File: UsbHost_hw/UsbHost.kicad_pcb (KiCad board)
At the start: 2 copper layers, 24 x 72 mm, 41 parts, among them Q1 LED_RGB, SW1 BUTTON

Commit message: + USBHost HW v3
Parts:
- removed C23: 1.8pF, Capacitors:CAP_0402
- removed R7: 51R, Resistors:RES_0603
- removed XL2: ST_SWD, Connectors:PLS-4
- added C11: 1u, Capacitors:CAP_0603, F.Cu at (169.8, 161.0)
- added C9: 18pF, Capacitors:CAP_0603, F.Cu at (188.3, 180.6)
- added DA2: MCP1700, SOT:SOT23-3, F.Cu at (169.4, 189.7)
- added Logo1: Logo, Pictures:Ostranna_16d9_13d5, F.Cu at (178.5, 135.8)
- added R4: 100R, Resistors:RES_0603, F.Cu at (173.0, 169.6)
- added XTAL1: 12MHz, Quartz:0503x4-4, F.Cu at (188.3, 176.4)
- C1: value 10n -> 18pF
- C12, C14: value 10pF -> 18pF
- C16, C21: value 220pF -> 0.1u
- C17, C19: value 10n -> 0.1u
- C18: value 3.3pF -> 0.1u
- C22: value 1.8pF -> 2.7pF
- C3: footprint Capacitors:CAP_0805 -> Capacitors:CAP_0603
- Q1: value LED_RGB -> LED_5050
- R1: value 1M -> 100R
- R3: value 51R -> 100R
- R6: value 51R -> 1k
- XL1: value CONN_3 -> CONN_6; footprint Connectors:PLS-3 -> Connectors:PLS-6
- moved C1 25.3 mm to (188.3, 172.3), turned to 0 degrees
- moved R1 25.0 mm to (173.0, 166.4)
- moved C13 23.3 mm to (169.3, 187.9)
- moved DA1 23.1 mm to (169.3, 189.9)
- moved C10 19.5 mm to (171.8, 189.7), turned to 90 degrees
- moved R6 15.1 mm to (184.8, 175.9)
- moved XL1 13.0 mm to (168.7, 184.2), turned to 90 degrees
- moved TP2 12.9 mm to (182.3, 171.7)
- moved C2 11.4 mm to (176.8, 182.6)
- moved C3 8.02 mm to (185.6, 179.8), turned to 270 degrees
- moved C8 1.68 mm to (184.0, 179.8), turned to 270 degrees
- moved C7 1.68 mm to (184.1, 173.6), turned to 90 degrees
- moved R2 0.91 mm to (188.1, 183.7)
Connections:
- C1 pad 1: /SHLD -> Net-(C1-Pad1)
- DD1 pad 10: (no net) -> Net-(DD1-Pad10)
- DD1 pad 11: (no net) -> Net-(DD1-Pad11)
- DD1 pad 2: (no net) -> Net-(DD1-Pad2)
- DD1 pad 20: (no net) -> Net-(DD1-Pad20)
- DD1 pad 21: (no net) -> Net-(DD1-Pad21)
- DD1 pad 22: (no net) -> Net-(DD1-Pad22)
- DD1 pad 25: (no net) -> Net-(DD1-Pad25)
- DD1 pad 26: (no net) -> Net-(DD1-Pad26)
- DD1 pad 27: (no net) -> Net-(DD1-Pad27)
- DD1 pad 28: (no net) -> Net-(DD1-Pad28)
- DD1 pad 29: (no net) -> Net-(DD1-Pad29)
- DD1 pad 3: (no net) -> Net-(DD1-Pad3)
- DD1 pad 38: (no net) -> Net-(DD1-Pad38)
- DD1 pad 39: (no net) -> Net-(DD1-Pad39)
- DD1 pad 4: (no net) -> Net-(DD1-Pad4)
- DD1 pad 41: (no net) -> Net-(DD1-Pad41)
- DD1 pad 42: (no net) -> Net-(DD1-Pad42)
- DD1 pad 43: (no net) -> Net-(DD1-Pad43)
- DD1 pad 45: (no net) -> Net-(DD1-Pad45)
- DD1 pad 46: (no net) -> Net-(DD1-Pad46)
- DD1 pad 5: (no net) -> Net-(C9-Pad1)
- DD1 pad 6: (no net) -> Net-(DD1-Pad6)
- DD1 pad 7: (no net) -> Net-(DD1-Pad7)
- R1 pad 1: /SHLD -> Net-(Q1-Pad1)
- R1 pad 2: GND -> /LED_G
- R3 pad 1: Net-(Q1-PadRA) -> Net-(Q1-Pad2)
- R6 pad 1: Net-(Q1-PadGA) -> Net-(C1-Pad1)
- R6 pad 2: /LED_G -> Net-(DD1-Pad6)
- XL1 pad 1: GND -> PwrMCU
- XL1 pad 2: /UART_TX -> /SWCLK
- XL1 pad 3: /UART_RX -> GND
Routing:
- net Net-(ANT1-Pad1): track 3.55 -> 140.8 mm
- net /SHLD: track 29.5 -> 0.00 mm, vias 2 -> 0
- net GND: track 327.8 -> 304.4 mm, vias 71 -> 68
- net Net-(C9-Pad1): track 0.00 -> 10.1 mm
- net /UART_RX: track 5.15 -> 9.96 mm
- net Net-(C1-Pad1): track 0.00 -> 4.66 mm
- net Net-(XL3-PadH4): track 0.00 -> 4.20 mm
- net Net-(XL3-PadH1): track 0.00 -> 4.20 mm
- net Net-(Q1-PadRA): track 2.75 -> 0.00 mm
- net Net-(Q1-PadGA): track 2.75 -> 0.00 mm
- net Net-(Q1-PadBA): track 2.75 -> 0.00 mm
- net Net-(Q1-Pad3): track 0.00 -> 2.75 mm
- net Net-(Q1-Pad2): track 0.00 -> 2.75 mm
- net Net-(Q1-Pad1): track 0.00 -> 2.75 mm
- net Net-(DD1-Pad6): track 0.00 -> 2.00 mm
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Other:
- board text added: "Ostranna UsbHost 3"

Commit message: + USBHost 4
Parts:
- removed C1, C9: 18pF, Capacitors:CAP_0603
- removed DA1: NCP583SQ, SOT:SC82AB
- removed R6: 1k, Resistors:RES_0603
- removed XTAL1: 12MHz, Quartz:0503x4-4
- added Logo3: Logo, Pictures:MadeInRussia_22d8, B.Cu at (179.0, 149.5)
- ANT1: footprint Radio:ANT_868_SEIDHE -> Antennas:ANT_868_SEIDHE
- Logo1: footprint Pictures:Ostranna_16d9_13d5 -> Pictures:KvantduinoLogoText_26d6
- moved DA2 1.00 mm to (169.3, 190.7)
- moved Logo1 0.94 mm to (178.9, 136.6), turned to 270 degrees
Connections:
- DD1 pad 10: Net-(DD1-Pad10) -> (no net)
- DD1 pad 11: Net-(DD1-Pad11) -> (no net)
- DD1 pad 2: Net-(DD1-Pad2) -> (no net)
- DD1 pad 20: Net-(DD1-Pad20) -> (no net)
- DD1 pad 21: Net-(DD1-Pad21) -> (no net)
- DD1 pad 22: Net-(DD1-Pad22) -> (no net)
- DD1 pad 25: Net-(DD1-Pad25) -> (no net)
- DD1 pad 26: Net-(DD1-Pad26) -> (no net)
- DD1 pad 27: Net-(DD1-Pad27) -> (no net)
- DD1 pad 28: Net-(DD1-Pad28) -> (no net)
- DD1 pad 29: Net-(DD1-Pad29) -> (no net)
- DD1 pad 3: Net-(DD1-Pad3) -> (no net)
- DD1 pad 38: Net-(DD1-Pad38) -> (no net)
- DD1 pad 39: Net-(DD1-Pad39) -> (no net)
- DD1 pad 4: Net-(DD1-Pad4) -> (no net)
- DD1 pad 41: Net-(DD1-Pad41) -> (no net)
- DD1 pad 42: Net-(DD1-Pad42) -> (no net)
- DD1 pad 43: Net-(DD1-Pad43) -> (no net)
- DD1 pad 45: Net-(DD1-Pad45) -> (no net)
- DD1 pad 46: Net-(DD1-Pad46) -> (no net)
- DD1 pad 5: Net-(C9-Pad1) -> (no net)
- DD1 pad 6: Net-(DD1-Pad6) -> (no net)
- DD1 pad 7: Net-(DD1-Pad7) -> (no net)
- XL1 pad 1: PwrMCU -> (no net)
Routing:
- net Net-(C9-Pad1): track 10.1 -> 0.00 mm
- net Net-(C1-Pad1): track 4.66 -> 0.00 mm
- net GND: track 304.4 -> 301.9 mm, vias 68 -> 67
- net +5V: track 20.2 -> 18.1 mm
- net Net-(DD1-Pad6): track 2.00 -> 0.00 mm
- net +3.3V: track 143.0 -> 143.2 mm, vias 12 -> 13
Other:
- board text removed: "Ostranna UsbHost 3"

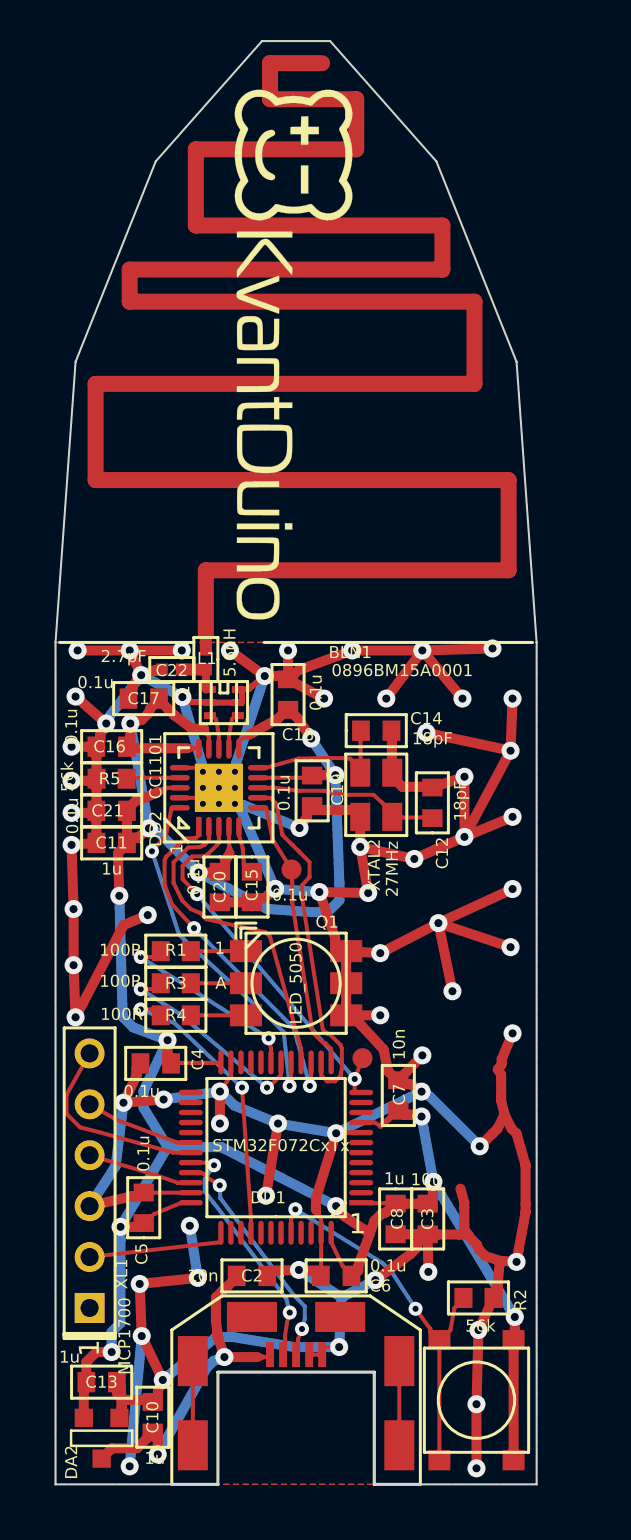
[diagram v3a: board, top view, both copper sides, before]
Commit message: + USBHost 5
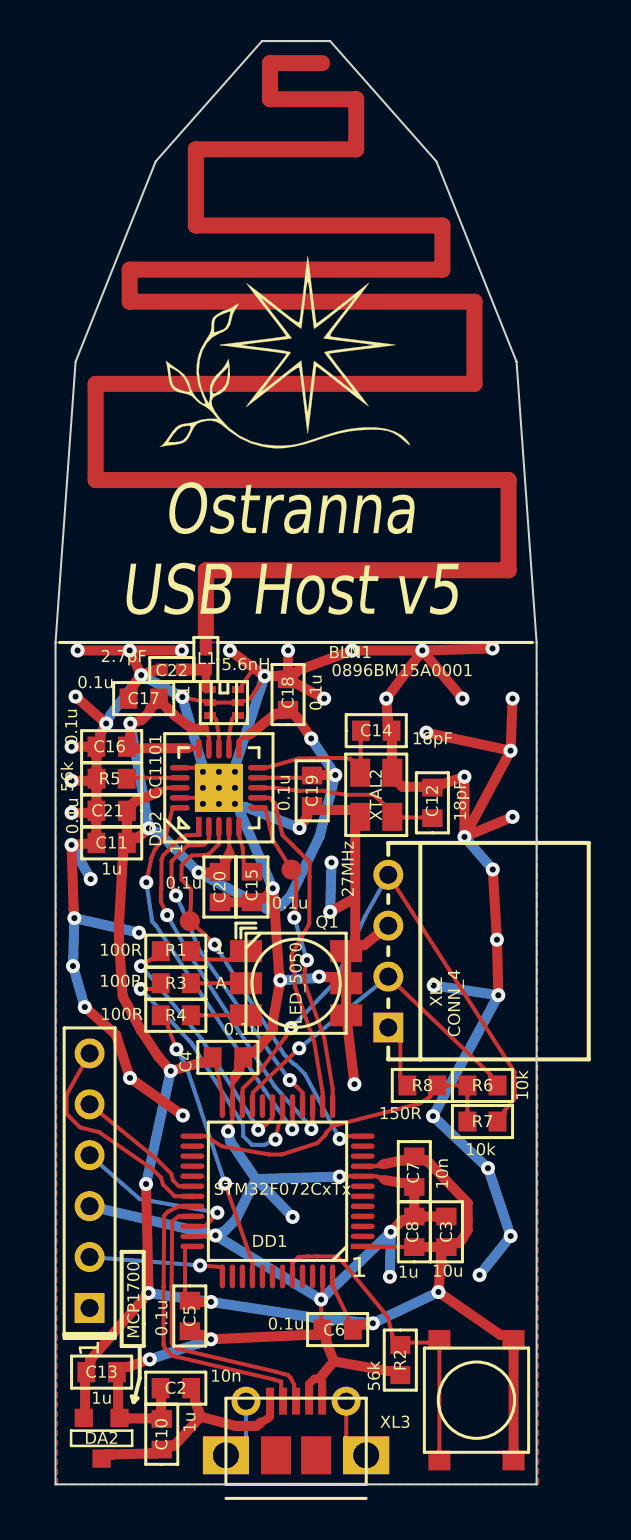
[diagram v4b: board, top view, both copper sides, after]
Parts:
- removed Logo3: Logo, Pictures:MadeInRussia_22d8
- added R6: 10k, Resistors:RES_0603, F.Cu at (188.3, 173.1)
- added R7: 10k, Resistors:RES_0603, F.Cu at (188.3, 174.9)
- added R8: 150R, Resistors:RES_0603, F.Cu at (185.3, 173.1)
- added XL2: CONN_4, Connectors:PBS-4R, F.Cu at (183.6, 166.4)
- Logo1: footprint Pictures:KvantduinoLogoText_26d6 -> Pictures:Ostranna_12d7_10d1
- XL3: footprint Connectors:USBmicro_MOLEX_WM17142 -> Connectors:USBmicro_MOLEX_1050170001
- moved TP2 11.0 mm to (173.7, 164.9)
- moved C2 6.77 mm to (173.0, 188.2), turned to 0 degrees
- moved C5 5.87 mm to (173.7, 184.6), turned to 270 degrees
- moved XL3 5.60 mm to (179.0, 193.0), turned to 0 degrees
- moved R2 4.98 mm to (184.2, 186.8), turned to 270 degrees
- moved C7 3.88 mm to (184.9, 177.4), turned to 270 degrees
- moved C4 3.61 mm to (175.6, 171.7), turned to 0 degrees
- moved C6 2.68 mm to (181.1, 185.3)
- moved DD1 2.18 mm to (178.1, 178.4)
- moved C8 1.13 mm to (184.9, 180.4), turned to 90 degrees
- moved C3 1.13 mm to (186.5, 180.4), turned to 90 degrees
- moved C10 0.96 mm to (172.3, 190.5)
- moved Logo1 0.51 mm to (178.4, 136.5), turned to 0 degrees
- moved C13 0.50 mm to (169.3, 187.4)
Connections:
- DD1 pad 21: (no net) -> /SCL_PILL
- DD1 pad 22: (no net) -> /SDA_PILL
- DD1 pad 25: (no net) -> /PWR_PILL
- XL3 pad H2: (no net) -> Net-(XL3-PadH2)
- XL3 pad H3: (no net) -> Net-(XL3-PadH3)
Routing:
- net GND: track 301.9 -> 270.4 mm, vias 67 -> 57
- net /SDA_PILL: track 0.00 -> 28.4 mm, vias 0 -> 1
- net /SCL_PILL: track 0.00 -> 17.3 mm, vias 0 -> 1
- net /PWR_PILL: track 0.00 -> 16.8 mm
- net +5V: track 18.1 -> 11.8 mm, vias 2 -> 0
- net /SWDIO: track 5.26 -> 8.80 mm, vias 0 -> 1
- net /PWR_PILL_PROT: track 0.00 -> 3.26 mm
- net Net-(DD1-Pad44): track 19.7 -> 16.6 mm, vias 2 -> 0
- net /LED_R: track 10.7 -> 13.8 mm
- net /D-: track 12.2 -> 15.3 mm, vias 2 -> 0
- net /D+: track 11.6 -> 14.7 mm, vias 2 -> 0
- net /LED_G: track 9.88 -> 12.9 mm
- net +3.3V: track 143.2 -> 140.7 mm, vias 13 -> 11
- net /CC_GDO0: track 13.9 -> 15.9 mm, vias 0 -> 2
- net /CC_SCK: track 17.7 -> 19.7 mm
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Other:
- outline, holes or cut-outs redrawn
- net class Wide: via_dia 0.9 -> 0.7; via_drill 0.4 -> 0.3
- board text added: "Ostranna USB Host v5"
